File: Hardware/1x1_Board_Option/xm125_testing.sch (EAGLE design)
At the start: 26 parts, among them J1 QWIIC_RIGHT_ANGLE, J2 QWIIC_RIGHT_ANGLE

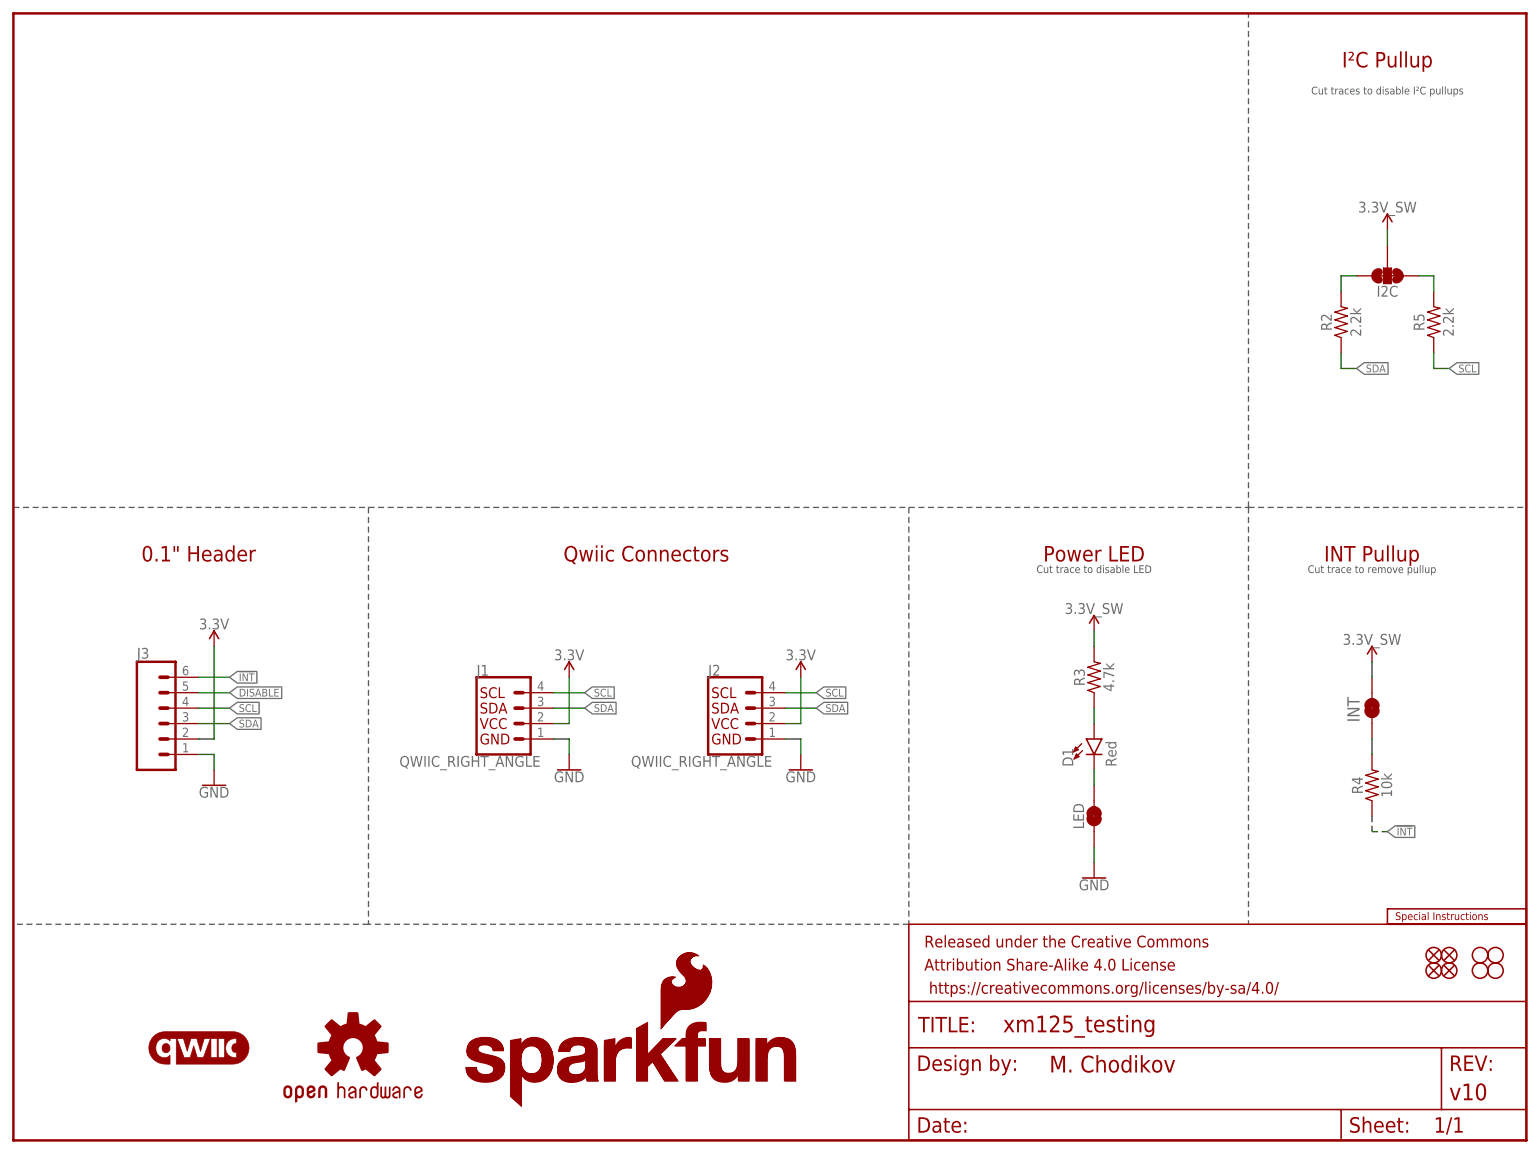
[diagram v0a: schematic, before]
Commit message: Addition of initial Hardware files for breakout
We will be doing a breakout with this board, no need for 1x1 and thing+ breakout files. Will be keeping until official product definition is given
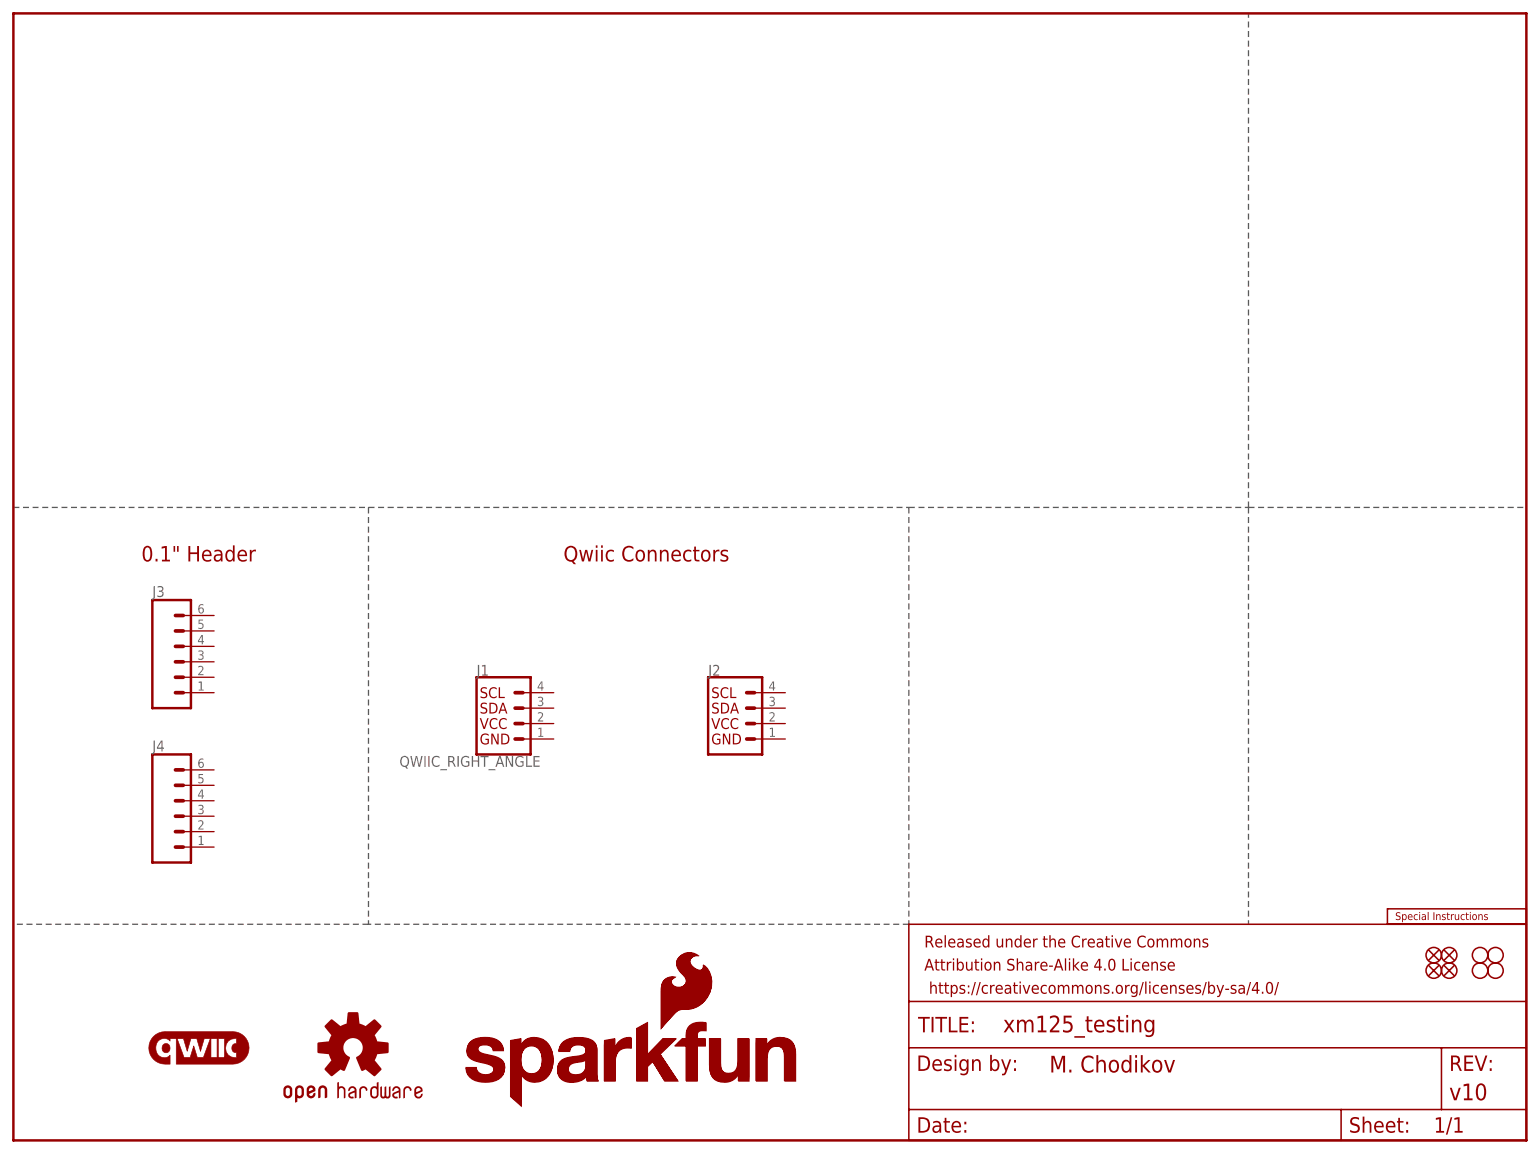
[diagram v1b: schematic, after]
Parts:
- removed D1: Red, SparkFun-LED:LED-RED_0603-KB
- removed I2C: JUMPER-SMT_3_2-NC_TRACE_SILK, SparkFun-Jumpers:JUMPER-SMT_3_2-NC_TRACE_SILK
- removed JP2, LED: JUMPER-SMT_2_NC_TRACE_SILK, SparkFun-Jumpers:JUMPER-SMT_2_NC_TRACE_SILK
- removed R2, R5: 2.2k, SparkFun-Resistors:2.2KOHM-0603-1/10W-1%
- removed R3: 4.7k, SparkFun-Resistors:4.7KOHM-0603-1/10W-1%
- removed R4: 10k, SparkFun-Resistors:10KOHM-0603-1/10W-1%
- added J4: (no value), SparkFun-Connectors:CONN_06NO_SILK_FEMALE_PTH
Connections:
- removed net !INT: J3.6, R4.1
- removed net 3.3V: J1.2, J2.2, J3.2
- removed net 3.3V_SW: I2C.2, JP2.2, R3.2
- removed net DISABLE: J3.5
- removed net GND: J1.1, J2.1, J3.1, LED.1
- removed net N$1: D1.C, LED.2
- removed net N$2: I2C.3, R2.2
- removed net N$4: D1.A, R3.1
- removed net N$5: JP2.1, R4.2
- removed net N$6: I2C.1, R5.2
- removed net SCL: J1.4, J2.4, J3.4, R5.1
- removed net SDA: J1.3, J2.3, J3.3, R2.1
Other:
- note removed: "Cut trace to disable LED"
- note removed: "Cut trace to remove pullup"
- note removed: "Cut traces to disable I²C pullups"
- note removed: "INT"
- note removed: "INT Pullup"
- note removed: "I²C Pullup"
- note removed: "Power LED"
- moved on the sheet: J3
